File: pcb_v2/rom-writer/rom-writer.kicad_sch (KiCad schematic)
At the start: 25 parts, among them J1 cartridge, Q1 IRF540N, U1 74LS574, U2 74LS574, U4 74LS125

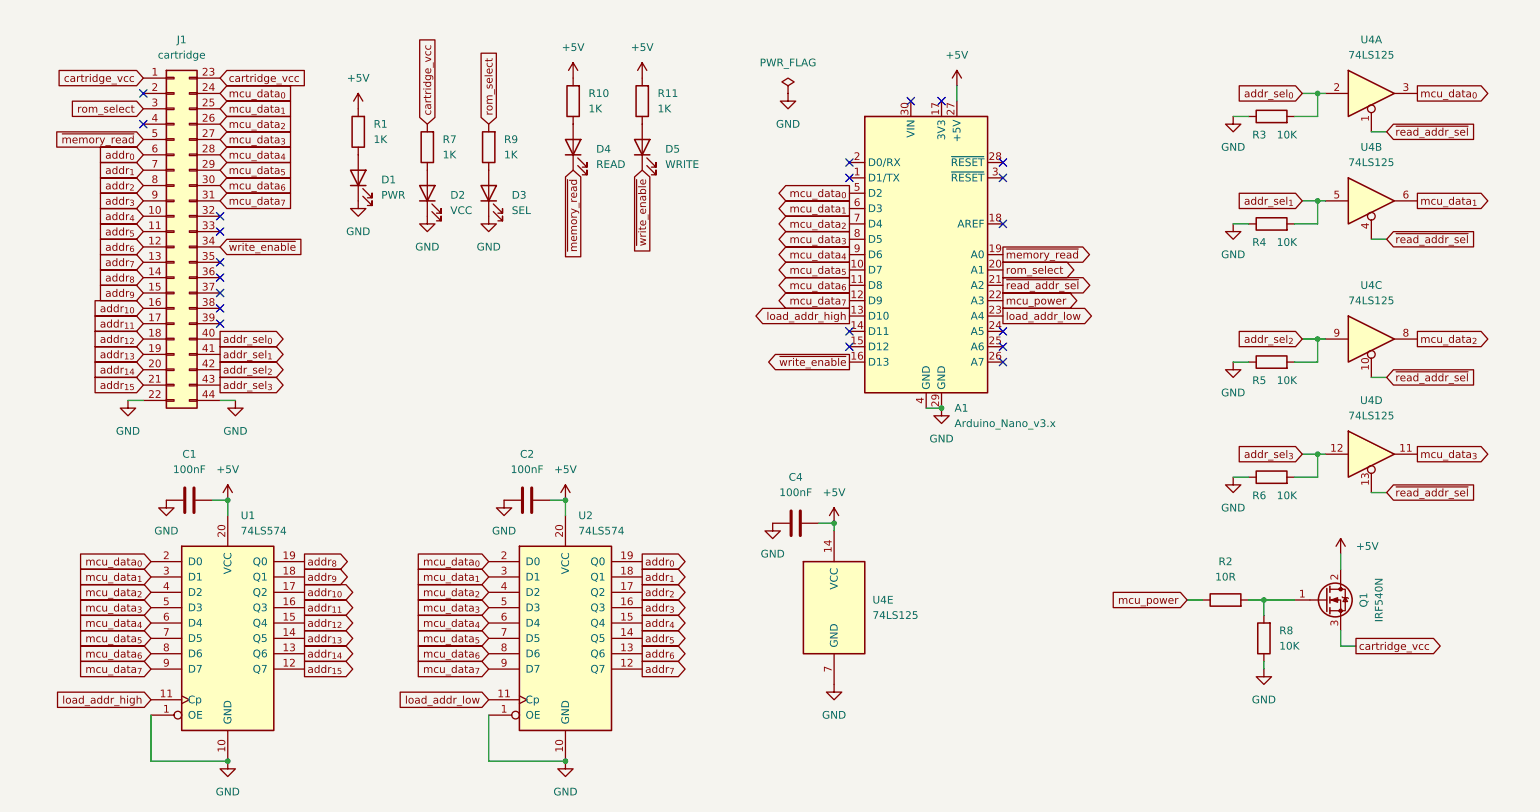
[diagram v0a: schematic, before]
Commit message: seleção de chip de rom feita pela placa de memória; isso reduz um chip no cartucho
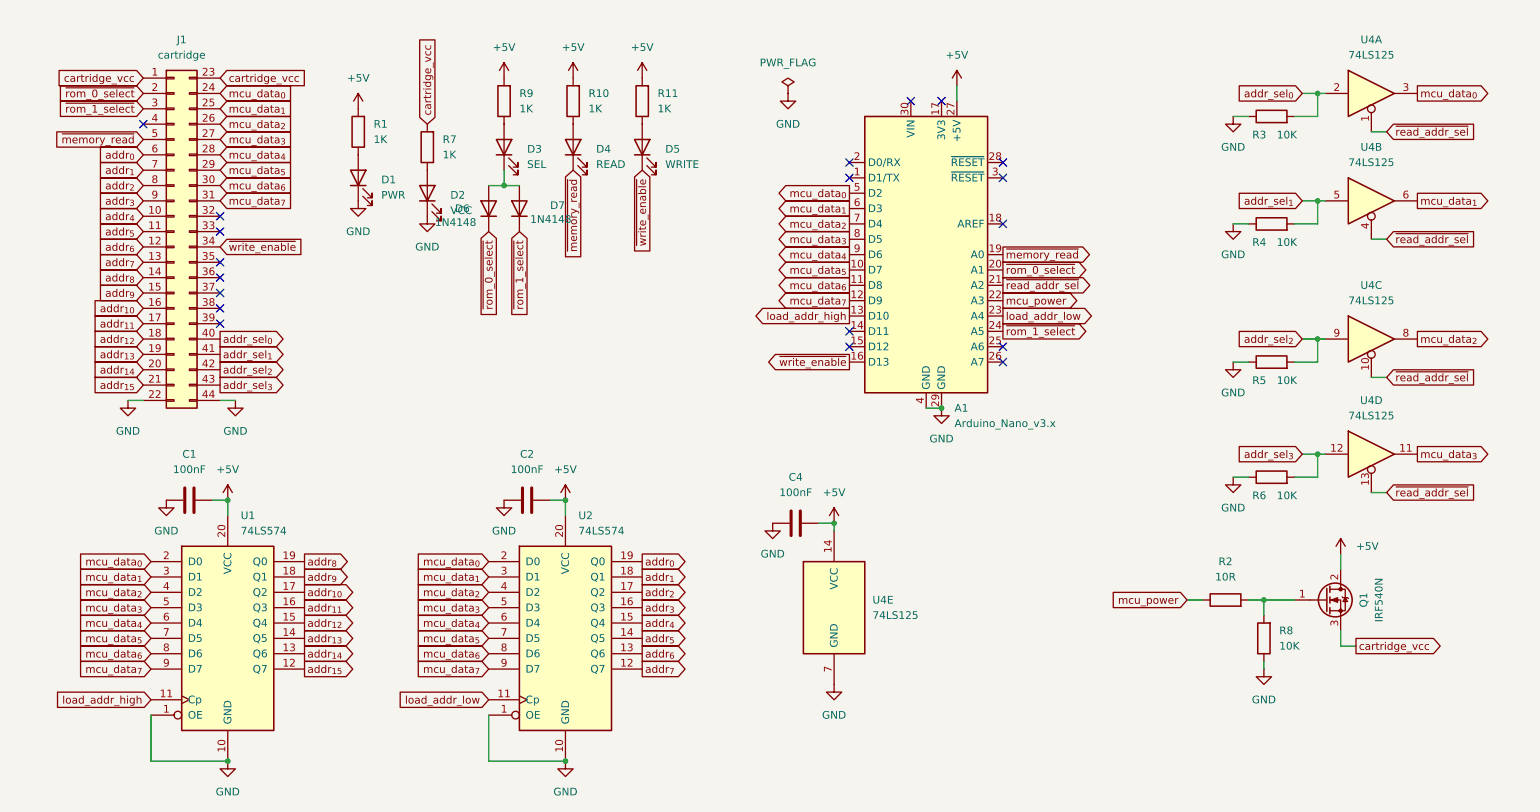
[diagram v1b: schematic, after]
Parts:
- added D6, D7: 1N4148, Diode_THT:D_DO-35_SOD27_P7.62mm_Horizontal, symbol Diode:1N4148
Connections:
- net +5V: now also R9.2
- net GND: no longer D3.1 (K)
- net ~{rom_0_select}: now reaches J1.2 (Pin_2)
- net ~{rom_0_select}: now also A1.20 (A1), D6.1 (K)
- net ~{rom_1_select}: now reaches A1.24 (A5)
- net ~{rom_1_select}: now also J1.3 (Pin_3), D7.1 (K)
- removed net rom_select: A1.20 (A1), J1.3 (Pin_3), R9.2
- new net: D3.1 (K), D6.2 (A), D7.2 (A)
- no-connect marks 21 -> 19
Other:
- moved on the sheet: D3, R9
